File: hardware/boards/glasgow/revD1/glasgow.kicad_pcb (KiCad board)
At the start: 6 copper layers, 95 x 55 mm, 722 parts, among them J1 USB-C, J10 P1, J2 SWD, J3 COM, J4 SYNC, J5 JTAG, J6 LVDS, J7 P1, J8 P1, J9 P1, Q1 AO3401, Q2 AO3400, SW1 RST, U1 BL24C256A-SFRC, U10 74AXP1T45, U11 XccelaOPI, U12 XccelaOPI, U13 TLV62569PDRL, U14 TLV62569PDRL, U15 TLV61070ADBV, U16 APX811-40UG-7, U17 TLV77525DRL, U18 TLV62569PDRL, U19 TPS7A2033, U2 CY7C68013A-56LTX, U20 TPS22917DBV, U21 DAC43204, U22 SY8301, U23 SY7208CABC, U24 PCA6416APW, U25 PCA6416APW, U26 74AXP1T45, U27 74AXP1T45, U28 TPS629203, U29 74AXP1T45, U3 TMP112xxDRL, U30 74AXP1T45, U31 74AXP1T45, U32 74AXP1T45, U33 NCP456R, U34 INA233, U35 74AXP1T45, U36 74AXP1T45, U37 TLV6001DCK, U38 74AXP1T45, U39 74AXP1T45, U4 FUSB302B01MPX, U40 TPS629203, U41 74AXP1T45, U42 74AXP1T45, U43 74AXP1T45, U44 74AXP1T45, U45 NCP456R, U46 INA233, U47 74AXP1T45, U48 74AXP1T45, U49 TLV6001DCK, U5 TPS259472ARPW, U50 74AXP1T45, U51 74AXP1T45, U52 TPS629203, U53 74AXP1T45, U54 74AXP1T45, U55 74AXP1T45, U56 74AXP1T45, U57 NCP456R, U58 INA233, U59 74AXP1T45, U6 STM32G031G6Ux, U60 74AXP1T45, U61 TLV6001DCK, U62 74AXP1T45, U63 74AXP1T45, U64 TPS629203, U65 74AXP1T45, U66 74AXP1T45, U67 74AXP1T45, U68 74AXP1T45, U69 NCP456R, U7 NAFE71388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

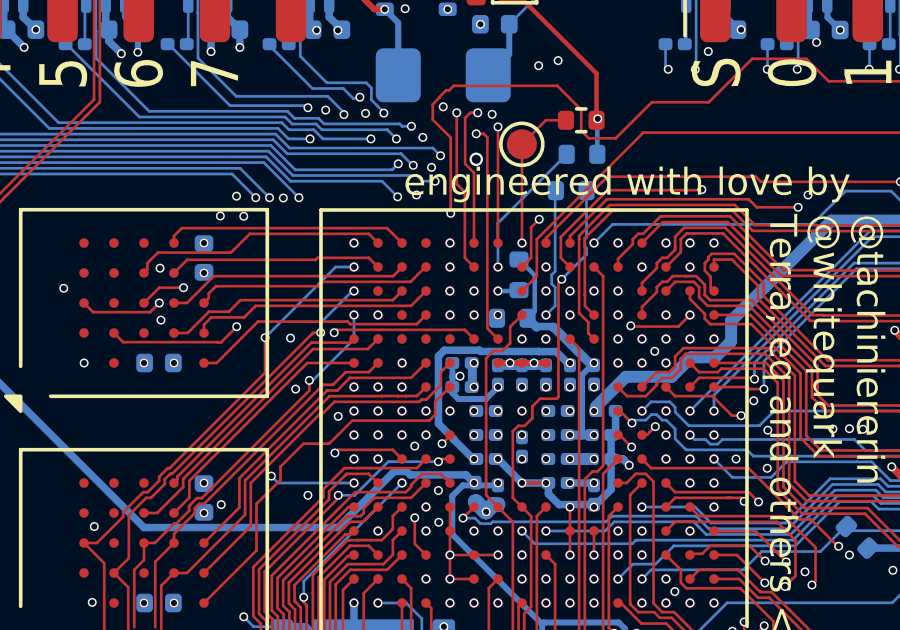
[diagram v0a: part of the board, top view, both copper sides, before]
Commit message: add the rest of mandatory testpoints
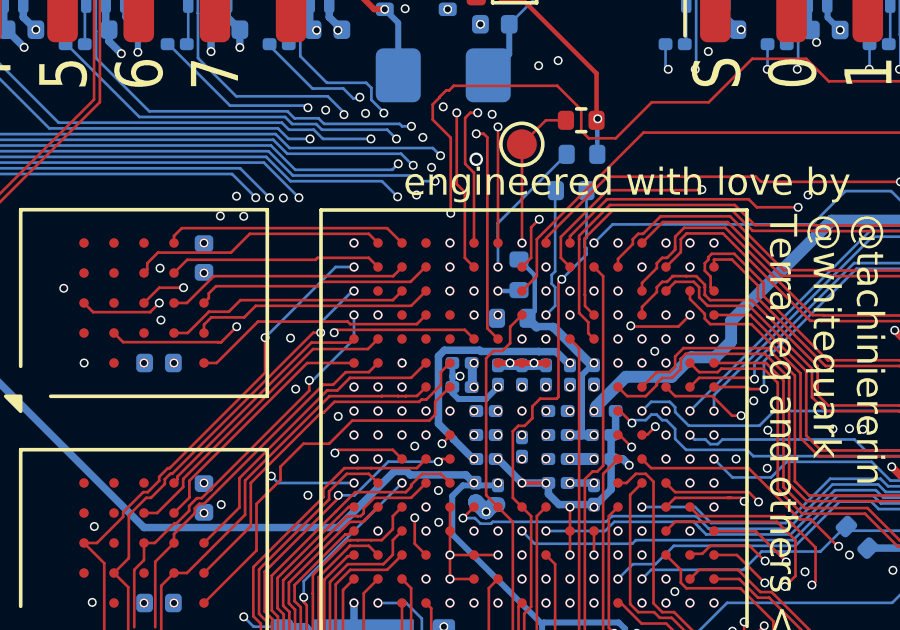
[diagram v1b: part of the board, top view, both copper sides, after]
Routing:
- net GND: vias 669 -> 668
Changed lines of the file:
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@@
-	)
-	(via
-		(at 193.725 85.39)
-		(size 0.3)
-		(drill 0.2)
-		(layers "F.Cu" "B.Cu")
-		(net "GND")
 	)
 	(via
